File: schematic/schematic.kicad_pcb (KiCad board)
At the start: 4 copper layers, 100 x 100 mm, 263 parts, among them J1 Conn_01x04, J10 Conn_01x03, J11 Conn_01x02, J12 Conn_01x02, J13 Conn_01x02, J14 Conn_01x02, J15 Conn_01x02, J16 Conn_01x02, J17 Conn_01x04, J18 Conn_02x13_Odd_Even, J19 Conn_02x05_Odd_Even, J2 Conn_01x04, J20 Conn_02x05_Odd_Even, J21 Conn_02x05_Odd_Even, J3 Conn_01x04, J4 Conn_01x04, J5 Conn_01x04, J6 Conn_01x06, J7 Conn_01x03, J8 Screw_Terminal_01x02, J9 Conn_01x03, Q1 PSMN1R7-30YL, Q2 PSMN1R7-30YL, Q3 NCV8402, Q4 NCV8402, SW1 SW_Push_Dual, SW2 SW_DIP_x03, U1 STM32F401VETx, U2 TMC2130, U3 TMC2130, U4 TMC2130, U5 TMC2130, U6 BD9E302EFJ, U7 BD9E302EFJ, U8 BD9E302EFJ, Y1 Crystal_GND24

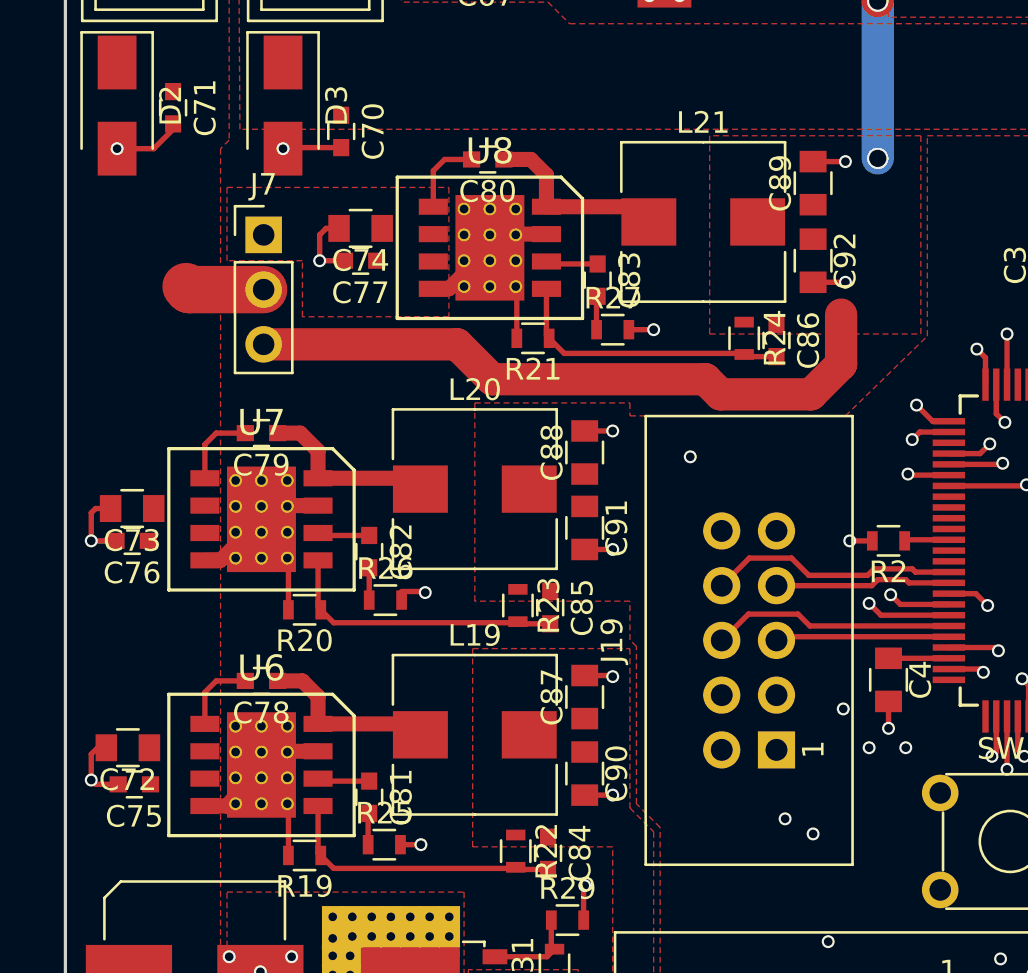
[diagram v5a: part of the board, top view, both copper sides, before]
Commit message: Changed footprint size of some capacitors
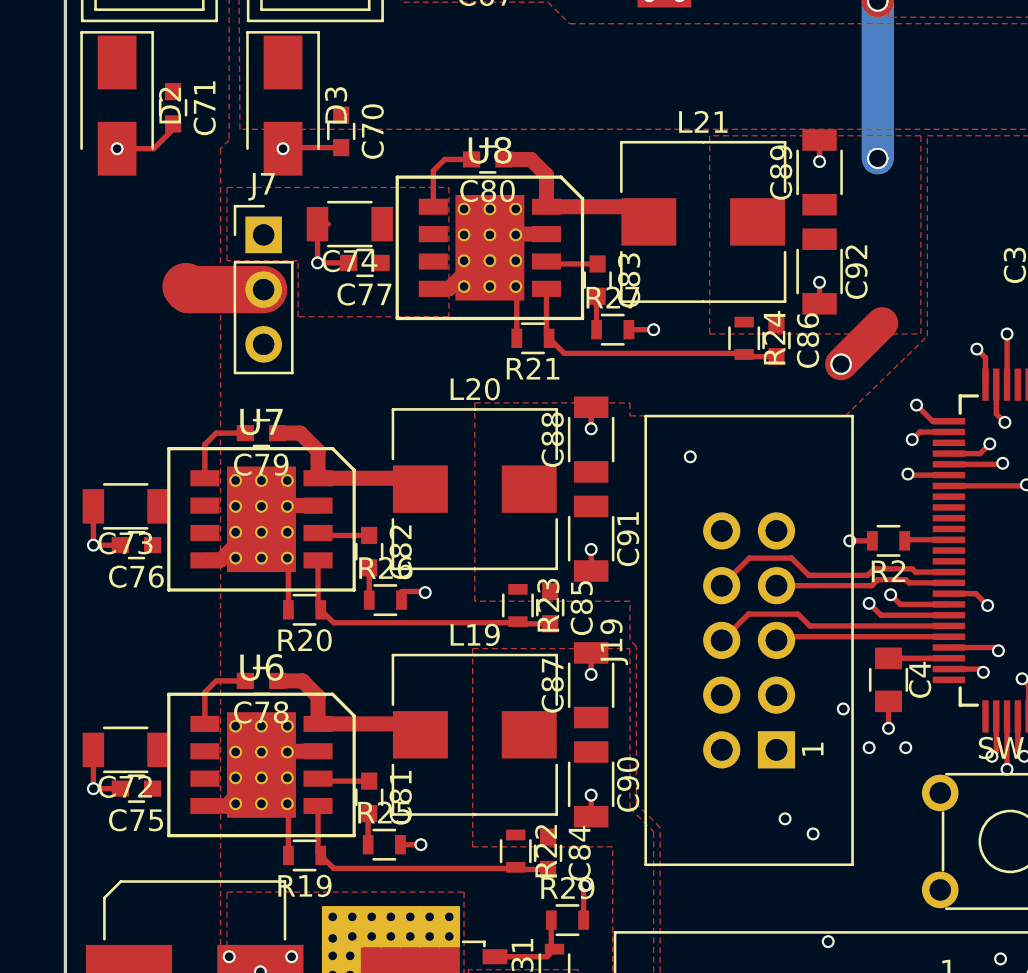
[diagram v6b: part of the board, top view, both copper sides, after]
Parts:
- C72, C73, C74, C87, C88, C89, C90, C91, C92: footprint Capacitors_SMD:C_0805 -> Capacitors_SMD:C_1206
- D12, D13, D14, D15: value BAT54S -> BAT54SW
- moved C88 0.67 mm to (189.4, 108.7)
- moved C87 0.63 mm to (189.4, 120.1)
- moved C89 0.58 mm to (200.0, 96.3)
- moved C90 0.58 mm to (189.4, 124.7)
- moved C91 0.58 mm to (189.4, 113.3)
- moved C92 0.58 mm to (200.0, 100.9)
- moved C74 0.54 mm to (178.2, 98.7)
- moved C73 0.32 mm to (167.8, 111.8)
- moved C76 0.28 mm to (168.3, 113.6)
- moved C77 0.22 mm to (178.9, 100.5)
- moved C75 0.22 mm to (168.3, 124.9)
- moved C72 0.14 mm to (167.8, 123.1)
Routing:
- net GND: track 405.2 -> 402.0 mm
- net +12V: track 119.8 -> 119.0 mm, vias 2 -> 3

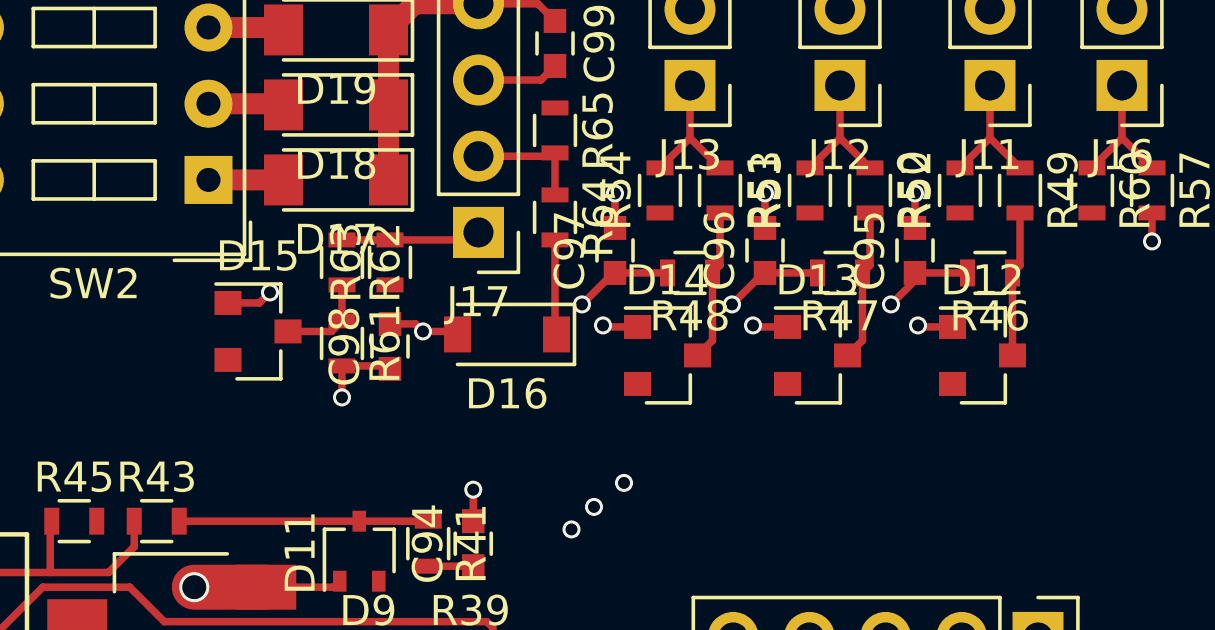
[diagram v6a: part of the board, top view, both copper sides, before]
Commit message: updated footprint bat54sw
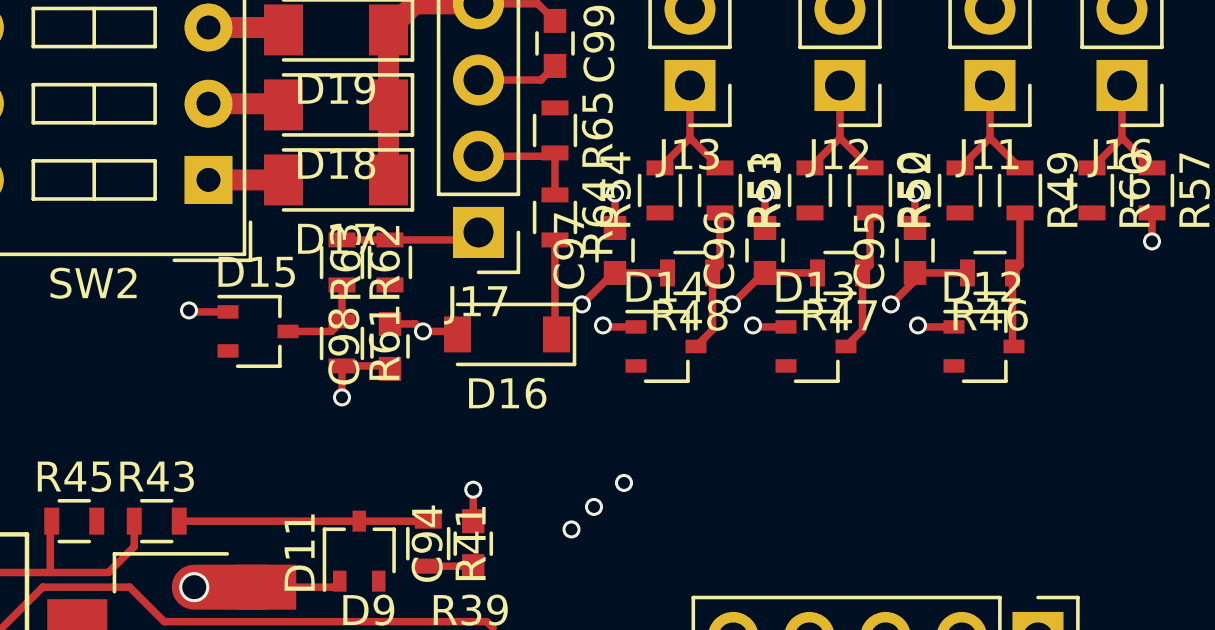
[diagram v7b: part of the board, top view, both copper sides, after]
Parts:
- D12, D13, D14, D15: footprint TO_SOT_Packages_SMD:SOT-23 -> TO_SOT_Packages_SMD:SOT-323_SC-70
- moved D12 0.30 mm to (241.8, 64.3)
- moved D13 0.30 mm to (236.2, 64.3)
- moved D14 0.30 mm to (231.2, 64.3)

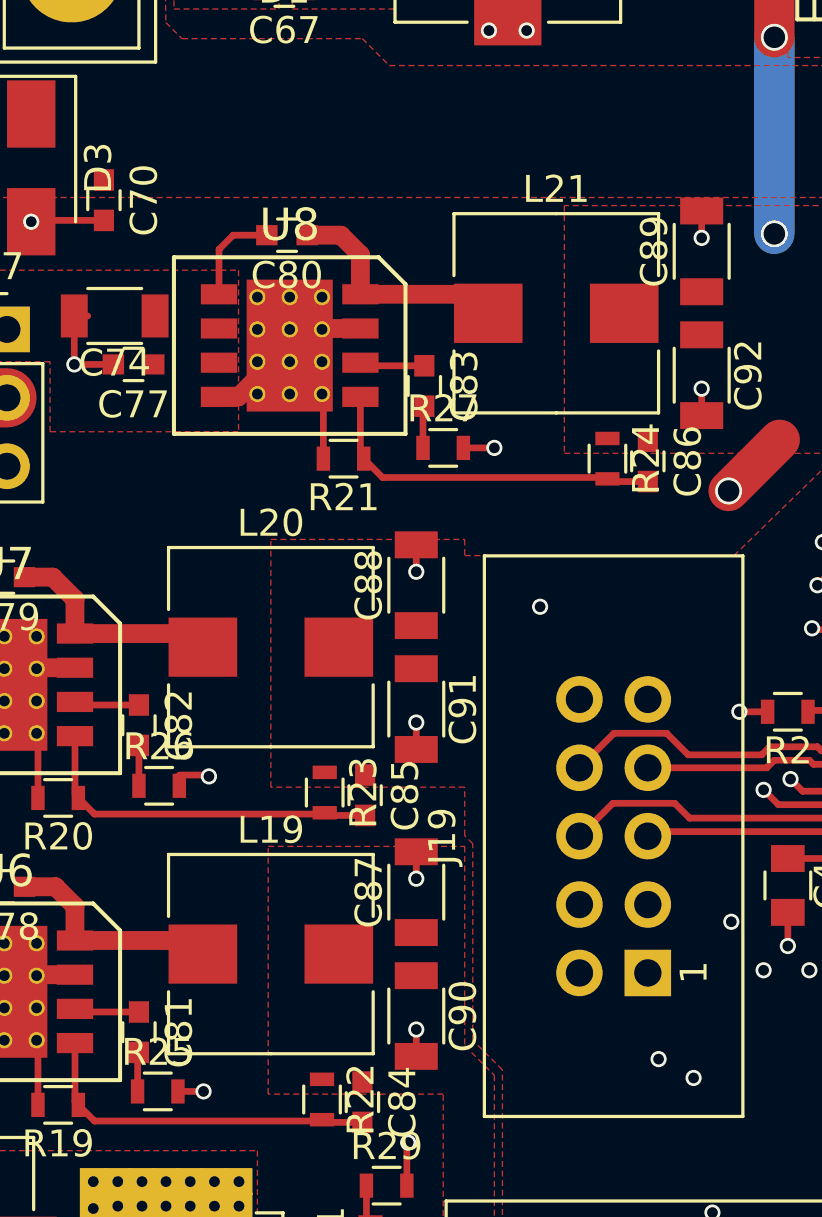
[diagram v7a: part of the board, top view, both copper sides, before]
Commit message: Updated inductor footprint
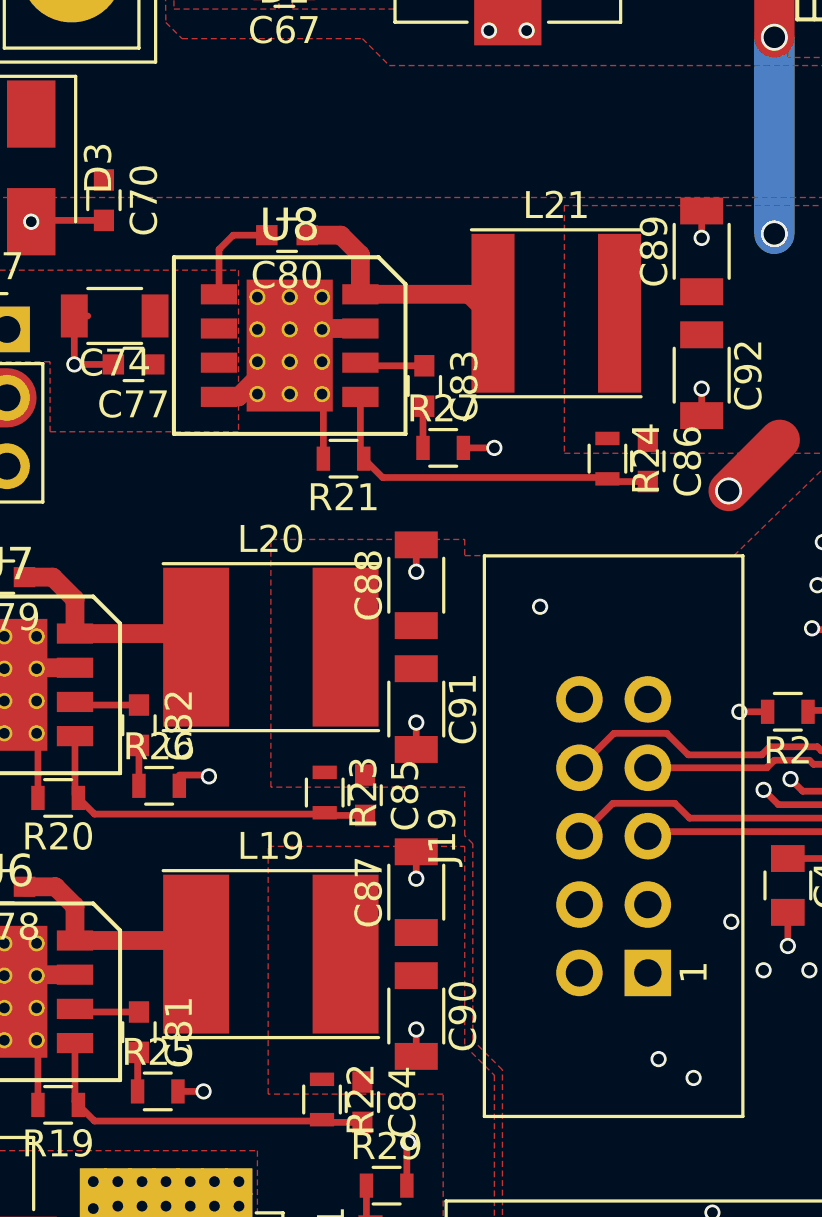
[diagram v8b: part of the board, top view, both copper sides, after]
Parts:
- L19, L20: footprint Inductors_SMD_GITHUB:L_Wuerth_HCM-7070 -> Inductors_SMD:L_Taiyo-Yuden_NR-60xx_HandSoldering
- L21: footprint Inductors_SMD_GITHUB:L_Wuerth_HCM-7070 -> Inductors_SMD:L_Taiyo-Yuden_NR-60xx
